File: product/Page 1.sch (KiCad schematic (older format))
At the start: 36 parts, among them J1 10118192-0001LF, J2 ARJM11A3, U1 AZ1117-3.3, U2 LAN8720A

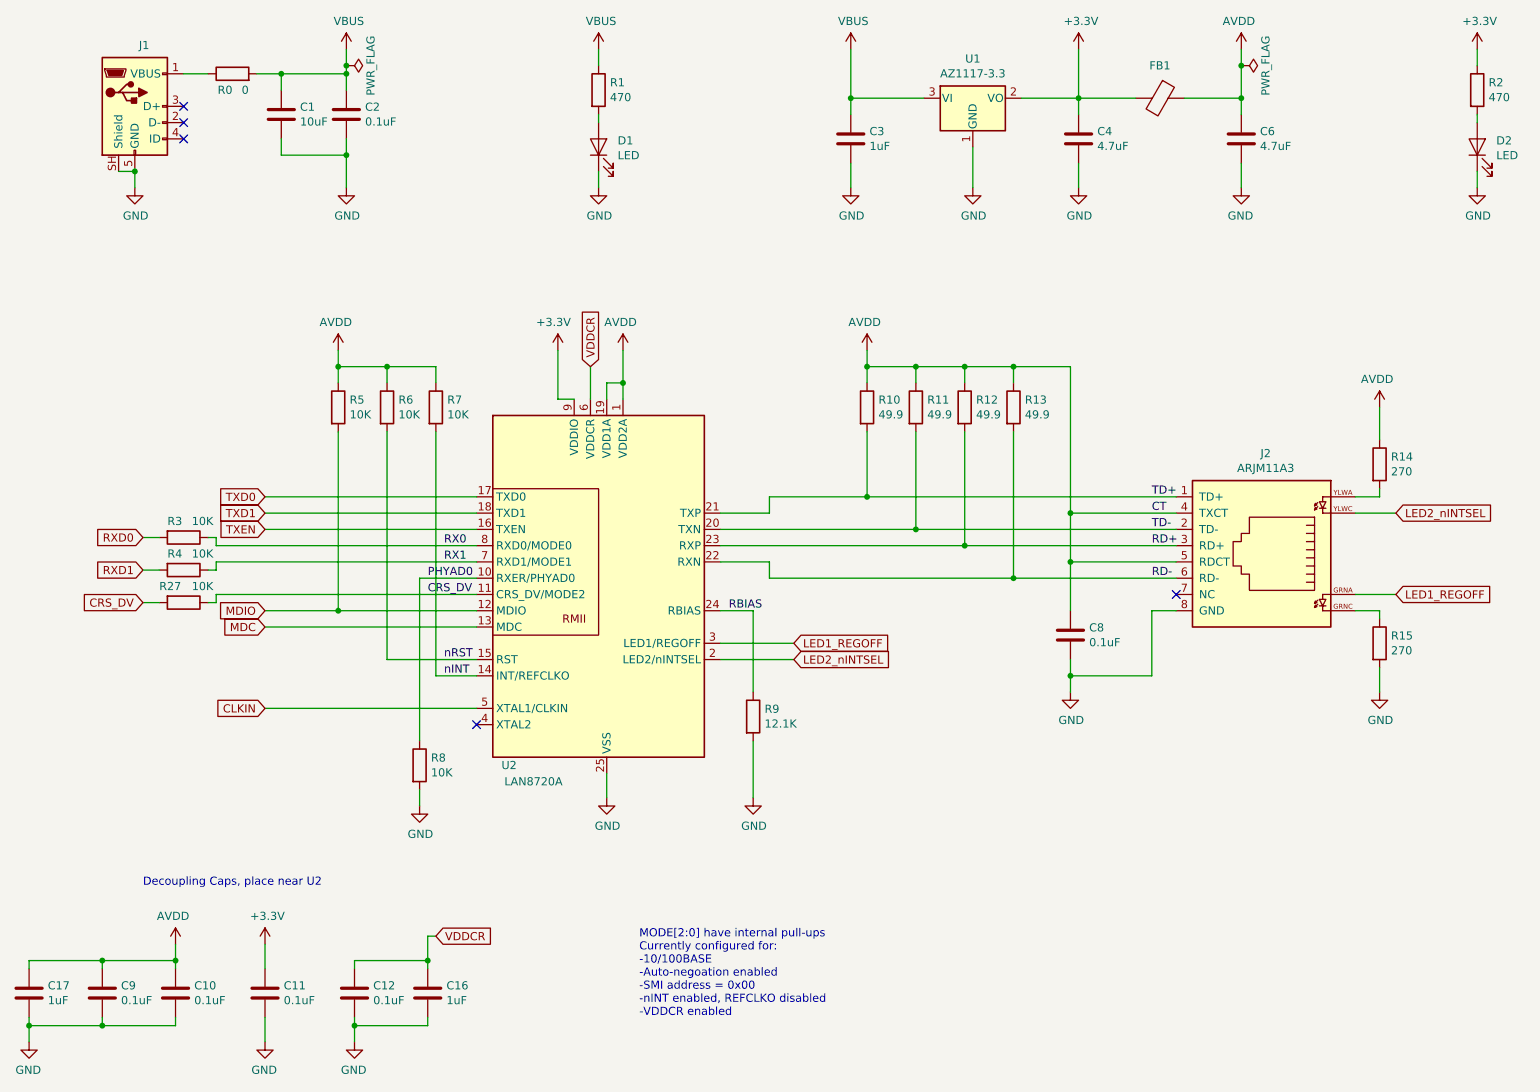
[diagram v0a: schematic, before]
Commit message: Added LCSC part numbers for product board
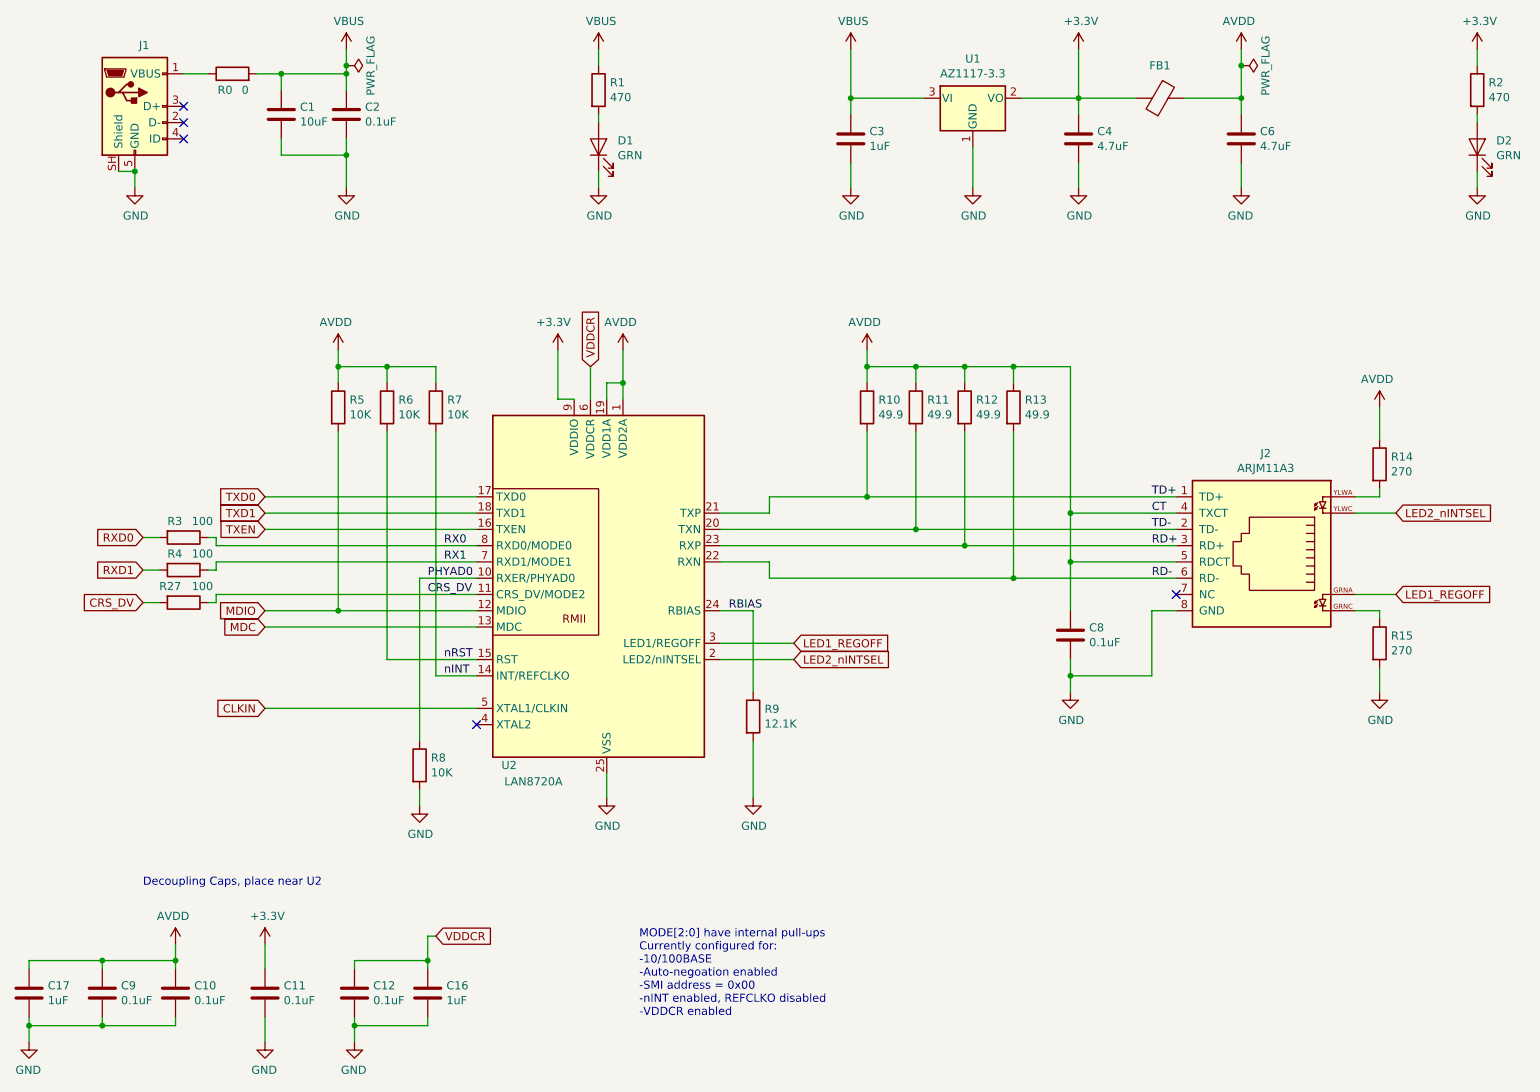
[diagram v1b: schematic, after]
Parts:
- C1: LCSC Part Number (none) -> C77044
- C10, C11, C12, C2, C8, C9: LCSC Part Number (none) -> C24452
- C16, C17, C3: LCSC Part Number (none) -> C1525
- C4, C6: LCSC Part Number (none) -> C99226
- D1, D2: value LED -> GRN; LCSC Part Number (none) -> C125094
- FB1: LCSC Part Number (none) -> C82850
- J1: LCSC Part Number (none) -> C132564
- R0: LCSC Part Number (none) -> C95177
- R1, R2: LCSC Part Number (none) -> C114433
- R10, R11, R12, R13: LCSC Part Number (none) -> C114625
- R14, R15: LCSC Part Number (none) -> C137641
- R27, R3, R4: value 10K -> 100; LCSC Part Number (none) -> C105588
- R5, R6, R7, R8: LCSC Part Number (none) -> C99198
- R9: LCSC Part Number (none) -> C123417
- U1: LCSC Part Number (none) -> C92517
- U2: LCSC Part Number (none) -> C45223
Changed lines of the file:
@@
 EESchema Schematic File Version 4
-LIBS:EsperDNS-cache
 EELAYER 30 0
 EELAYER END
@@
 F 2 "Capacitor_SMD:C_0603_1608Metric" H 2688 1500 50  0001 C CNN
 F 3 "~" H 2650 1650 50  0001 C CNN
+F 4 "C77044" H 2650 1650 50  0001 C CNN "LCSC Part Number"
 	1    2650 1650
 	1    0    0    -1
@@
 F 2 "Capacitor_SMD:C_0603_1608Metric" H 3088 1500 50  0001 C CNN
 F 3 "~" H 3050 1650 50  0001 C CNN
+F 4 "C24452" H 3050 1650 50  0001 C CNN "LCSC Part Number"
 	1    3050 1650
 	1    0    0    -1
@@
 F 2 "Resistor_SMD:R_0603_1608Metric" V 4530 1500 50  0001 C CNN
 F 3 "~" H 4600 1500 50  0001 C CNN
+F 4 "C114433" H 4600 1500 50  0001 C CNN "LCSC Part Number"
 	1    4600 1500
 	1    0    0    -1
@@
 AR Path="/5DED2F9B/5DF04BE6" Ref="D1"  Part="1"
 F 0 "D1" V 4639 1733 50  0000 R CNN
-F 1 "LED" V 4548 1733 50  0000 R CNN
+F 1 "GRN" V 4548 1733 50  0000 R CNN
 F 2 "Diode_SMD:D_0603_1608Metric" H 4600 1850 50  0001 C CNN
 F 3 "~" H 4600 1850 50  0001 C CNN
+F 4 "C125094" H 4600 1850 50  0001 C CNN "LCSC Part Number"
 	1    4600 1850
 	0    -1   -1   0
@@
 F 2 "Package_TO_SOT_SMD:SOT-223" H 6900 1800 50  0001 C CIN
 F 3 "https://www.diodes.com/assets/Datasheets/AZ1117.pdf" H 6900 1550 50  0001 C CNN
+F 4 "C92517" H 6900 1550 50  0001 C CNN "LCSC Part Number"
 	1    6900 1550
 	1    0    0    -1
@@
 F 2 "Capacitor_SMD:C_0603_1608Metric" H 6188 1650 50  0001 C CNN
 F 3 "~" H 6150 1800 50  0001 C CNN
+F 4 "C1525" H 6150 1800 50  0001 C CNN "LCSC Part Number"
 	1    6150 1800
 	1    0    0    -1
@@
 F 2 "Inductor_SMD:L_0603_1608Metric" V 7980 1550 50  0001 C CNN
 F 3 "~" H 8050 1550 50  0001 C CNN
+F 4 "C82850" H 8050 1550 50  0001 C CNN "LCSC Part Number"
 	1    8050 1550
 	0    1    1    0
@@
 F 2 "Capacitor_SMD:C_0603_1608Metric" H 7588 1650 50  0001 C CNN
 F 3 "~" H 7550 1800 50  0001 C CNN
+F 4 "C99226" H 7550 1800 50  0001 C CNN "LCSC Part Number"
 	1    7550 1800
 	1    0    0    -1
@@
 F 2 "Resistor_SMD:R_0603_1608Metric" V 9930 1500 50  0001 C CNN
 F 3 "~" H 10000 1500 50  0001 C CNN
+F 4 "C114433" H 10000 1500 50  0001 C CNN "LCSC Part Number"
 	1    10000 1500
 	1    0    0    -1
@@
 AR Path="/5DED2F9B/5DF04C4F" Ref="D2"  Part="1"
 F 0 "D2" V 10039 1733 50  0000 R CNN
-F 1 "LED" V 9948 1733 50  0000 R CNN
+F 1 "GRN" V 9948 1733 50  0000 R CNN
 F 2 "Diode_SMD:D_0603_1608Metric" H 10000 1850 50  0001 C CNN
 F 3 "~" H 10000 1850 50  0001 C CNN
+F 4 "C125094" H 10000 1850 50  0001 C CNN "LCSC Part Number"
 	1    10000 1850
 	0    -1   -1   0
@@
 F 2 "Package_DFN_QFN:QFN-24-1EP_4x4mm_P0.5mm_EP2.6x2.6mm" H 4700 3550 50  0001 L CNN
 F 3 "http://ww1.microchip.com/downloads/en/DeviceDoc/8720a.pdf" H 4450 3650 50  0001 C CNN
+F 4 "C45223" H 4650 4600 50  0001 C CNN "LCSC Part Number"
 	1    4650 4600
 	1    0    0    -1
@@
 F 2 "Resistor_SMD:R_0603_1608Metric" V 6480 3450 50  0001 C CNN
 F 3 "~" H 6550 3450 50  0001 C CNN
+F 4 "C114625" H 6550 3450 50  0001 C CNN "LCSC Part Number"
 	1    6550 3450
 	1    0    0    -1
@@
 F 2 "Resistor_SMD:R_0603_1608Metric" V 6780 3450 50  0001 C CNN
 F 3 "~" H 6850 3450 50  0001 C CNN
+F 4 "C114625" H 6850 3450 50  0001 C CNN "LCSC Part Number"
 	1    6850 3450
 	1    0    0    -1
@@
 F 2 "Resistor_SMD:R_0603_1608Metric" V 6180 3450 50  0001 C CNN
 F 3 "~" H 6250 3450 50  0001 C CNN
+F 4 "C114625" H 6250 3450 50  0001 C CNN "LCSC Part Number"
 	1    6250 3450
 	1    0    0    -1
@@
 F 2 "Resistor_SMD:R_0603_1608Metric" V 9330 3800 50  0001 C CNN
 F 3 "~" H 9400 3800 50  0001 C CNN
+F 4 "C137641" H 9400 3800 50  0001 C CNN "LCSC Part Number"
 	1    9400 3800
 	1    0    0    -1
@@
 F 2 "Resistor_SMD:R_0603_1608Metric" V 9330 4900 50  0001 C CNN
 F 3 "~" H 9400 4900 50  0001 C CNN
+F 4 "C137641" H 9400 4900 50  0001 C CNN "LCSC Part Number"
 	1    9400 4900
 	1    0    0    -1
@@
 F 2 "Capacitor_SMD:C_0603_1608Metric" H 7538 4700 50  0001 C CNN
 F 3 "~" H 7500 4850 50  0001 C CNN
+F 4 "C24452" H 7500 4850 50  0001 C CNN "LCSC Part Number"
 	1    7500 4850
 	-1   0    0    -1
@@
 F 2 "Resistor_SMD:R_0603_1608Metric" V 5480 5350 50  0001 C CNN
 F 3 "~" H 5550 5350 50  0001 C CNN
+F 4 "C123417" H 5550 5350 50  0001 C CNN "LCSC Part Number"
 	1    5550 5350
 	1    0    0    -1
@@
 F 2 "Resistor_SMD:R_0603_1608Metric" V 3430 5650 50  0001 C CNN
 F 3 "~" H 3500 5650 50  0001 C CNN
+F 4 "C99198" H 3500 5650 50  0001 C CNN "LCSC Part Number"
 	1    3500 5650
 	1    0    0    -1
@@
 F 2 "Resistor_SMD:R_0603_1608Metric" V 7080 3450 50  0001 C CNN
 F 3 "~" H 7150 3450 50  0001 C CNN
+F 4 "C114625" H 7150 3450 50  0001 C CNN "LCSC Part Number"
 	1    7150 3450
 	1    0    0    -1
@@
 F 2 "Capacitor_SMD:C_0603_1608Metric" H 8588 1650 50  0001 C CNN
 F 3 "~" H 8550 1800 50  0001 C CNN
+F 4 "C99226" H 8550 1800 50  0001 C CNN "LCSC Part Number"
 	1    8550 1800
 	-1   0    0    -1
@@
 F 2 "Resistor_SMD:R_0603_1608Metric" V 3530 3450 50  0001 C CNN
 F 3 "~" H 3600 3450 50  0001 C CNN
+F 4 "C99198" H 3600 3450 50  0001 C CNN "LCSC Part Number"
 	1    3600 3450
 	1    0    0    -1
@@
 F 2 "Resistor_SMD:R_0603_1608Metric" V 3230 3450 50  0001 C CNN
 F 3 "~" H 3300 3450 50  0001 C CNN
+F 4 "C99198" H 3300 3450 50  0001 C CNN "LCSC Part Number"
 	1    3300 3450
 	1    0    0    -1
@@
 F 2 "Resistor_SMD:R_0603_1608Metric" V 2930 3450 50  0001 C CNN
 F 3 "~" H 3000 3450 50  0001 C CNN
+F 4 "C99198" H 3000 3450 50  0001 C CNN "LCSC Part Number"
 	1    3000 3450
 	1    0    0    -1
@@
 F 2 "Resistor_SMD:R_0603_1608Metric" V 2280 1400 50  0001 C CNN
 F 3 "~" H 2350 1400 50  0001 C CNN
+F 4 "C95177" H 2350 1400 50  0001 C CNN "LCSC Part Number"
 	1    2350 1400
 	0    -1   -1   0
@@
 F 2 "Capacitor_SMD:C_0603_1608Metric" H 2038 6900 50  0001 C CNN
 F 3 "~" H 2000 7050 50  0001 C CNN
+F 4 "C24452" H 2000 7050 50  0001 C CNN "LCSC Part Number"
 	1    2000 7050
 	-1   0    0    -1
@@
 F 2 "Capacitor_SMD:C_0603_1608Metric" H 1588 6900 50  0001 C CNN
 F 3 "~" H 1550 7050 50  0001 C CNN
+F 4 "C24452" H 1550 7050 50  0001 C CNN "LCSC Part Number"
 	1    1550 7050
 	-1   0    0    -1
@@
 F 2 "Capacitor_SMD:C_0603_1608Metric" H 2588 6900 50  0001 C CNN
 F 3 "~" H 2550 7050 50  0001 C CNN
+F 4 "C24452" H 2550 7050 50  0001 C CNN "LCSC Part Number"
 	1    2550 7050
 	-1   0    0    -1
@@
 F 2 "Capacitor_SMD:C_0603_1608Metric" H 3138 6900 50  0001 C CNN
 F 3 "~" H 3100 7050 50  0001 C CNN
+F 4 "C24452" H 3100 7050 50  0001 C CNN "LCSC Part Number"
 	1    3100 7050
 	-1   0    0    -1
@@
 AR Path="/5DED2F9B/5DFE68F0" Ref="R3"  Part="1"
 F 0 "R3" V 1950 4150 50  0000 L CNN
-F 1 "10K" V 1950 4300 50  0000 L CNN
+F 1 "100" V 1950 4300 50  0000 L CNN
 F 2 "Resistor_SMD:R_0603_1608Metric" V 1980 4250 50  0001 C CNN
 F 3 "~" H 2050 4250 50  0001 C CNN
+F 4 "C105588" H 2050 4250 50  0001 C CNN "LCSC Part Number"
 	1    2050 4250
 	0    1    1    0
@@
 AR Path="/5DED2F9B/5DFE6B8F" Ref="R4"  Part="1"
 F 0 "R4" V 1950 4350 50  0000 L CNN
-F 1 "10K" V 1950 4500 50  0000 L CNN
+F 1 "100" V 1950 4500 50  0000 L CNN
 F 2 "Resistor_SMD:R_0603_1608Metric" V 1980 4450 50  0001 C CNN
 F 3 "~" H 2050 4450 50  0001 C CNN
+F 4 "C105588" H 2050 4450 50  0001 C CNN "LCSC Part Number"
 	1    2050 4450
 	0    1    1    0
@@
 F 2 "digikey-footprints:USB_Micro_B_Female_10118192" H 1900 1550 50  0001 C CNN
 F 3 "~" H 1900 1550 50  0001 C CNN
+F 4 "C132564" H 1750 1600 50  0001 C CNN "LCSC Part Number"
 	1    1750 1600
 	1    0    0    -1
@@
 F 2 "Capacitor_SMD:C_0603_1608Metric" H 3588 6900 50  0001 C CNN
 F 3 "~" H 3550 7050 50  0001 C CNN
+F 4 "C1525" H 3550 7050 50  0001 C CNN "LCSC Part Number"
 	1    3550 7050
 	-1   0    0    -1
@@
 F 2 "Capacitor_SMD:C_0603_1608Metric" H 1138 6900 50  0001 C CNN
 F 3 "~" H 1100 7050 50  0001 C CNN
+F 4 "C1525" H 1100 7050 50  0001 C CNN "LCSC Part Number"
 	1    1100 7050
 	-1   0    0    -1
@@
 AR Path="/5DED2F9B/5DFF908E" Ref="R27"  Part="1"
 F 0 "R27" V 1950 4500 50  0000 L CNN
-F 1 "10K" V 1950 4700 50  0000 L CNN
+F 1 "100" V 1950 4700 50  0000 L CNN
 F 2 "Resistor_SMD:R_0603_1608Metric" V 1980 4650 50  0001 C CNN
 F 3 "~" H 2050 4650 50  0001 C CNN
+F 4 "C105588" H 2050 4650 50  0001 C CNN "LCSC Part Number"
 	1    2050 4650
 	0    1    1    0

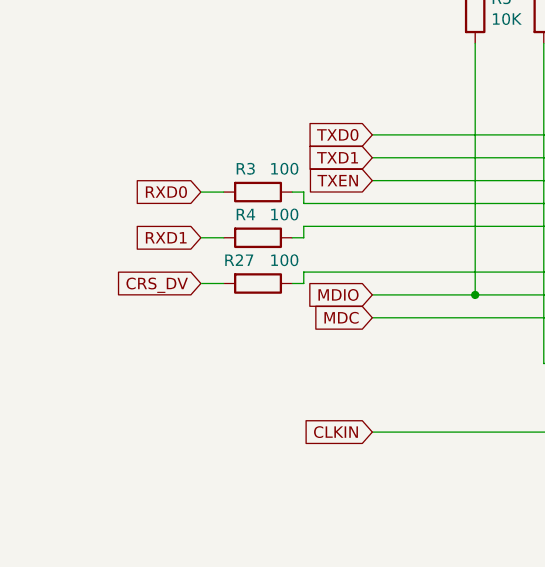
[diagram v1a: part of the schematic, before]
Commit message: Swapped TX & RX on Product Board
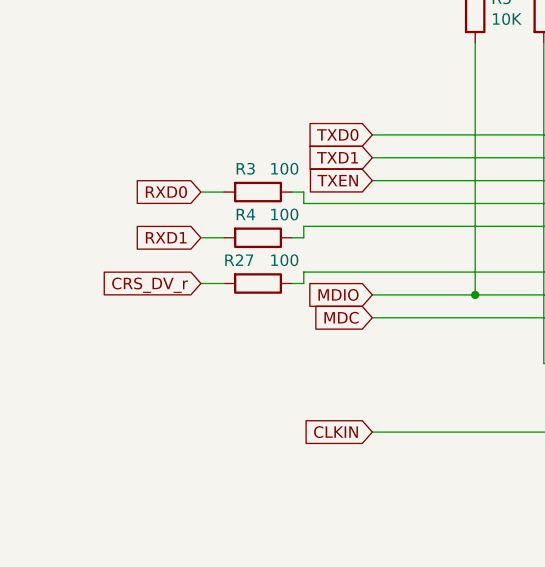
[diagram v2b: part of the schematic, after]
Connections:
- net CRS_DV: no longer R27.2
- new net CRS_DV_r: R27.2
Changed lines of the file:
@@
 MDIO
 Text GLabel 1800 4650 0    50   Input ~ 0
-CRS_DV
+CRS_DV_r
 Text GLabel 1800 4450 0    50   Input ~ 0
 RXD1
@@
 $EndComp
 Wire Wire Line
-	3500 4500 3500 5500
-Wire Wire Line
 	3500 5900 3500 5800
 $Comp
@@
 Wire Wire Line
 	2250 4650 2250 4600
-Wire Wire Line
-	2250 4600 3850 4600
 $Comp
 L Device:R R?
@@
 Text Label 3650 4400 0    50   ~ 0
 RX1
-Text Label 3550 4600 0    50   ~ 0
-CRS_DV
 $Comp
 L power:+3.3V #PWR?
@@
 	1    0    0    -1
 $EndComp
+Wire Wire Line
+	3500 4500 3500 5500
+Wire Wire Line
+	2250 4600 3850 4600
+Text Label 3550 4600 0    50   ~ 0
+CRS_DV
 $EndSCHEMATC

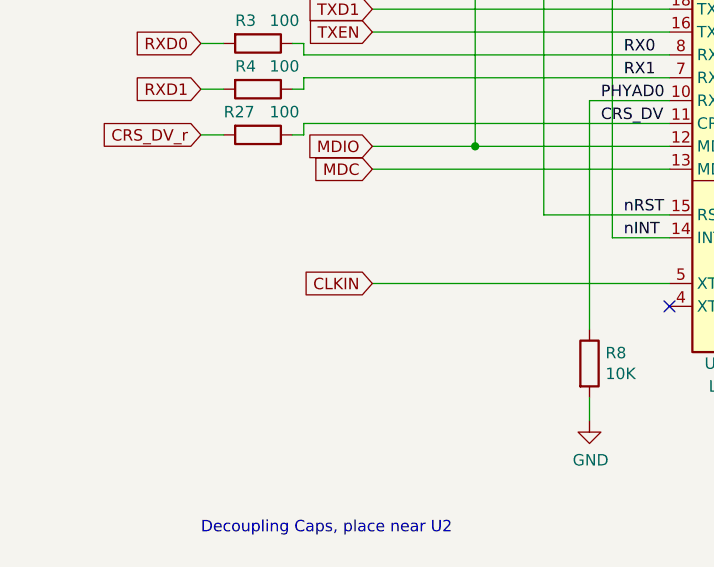
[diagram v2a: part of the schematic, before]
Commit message: Removed oscillator, replaced with IO17
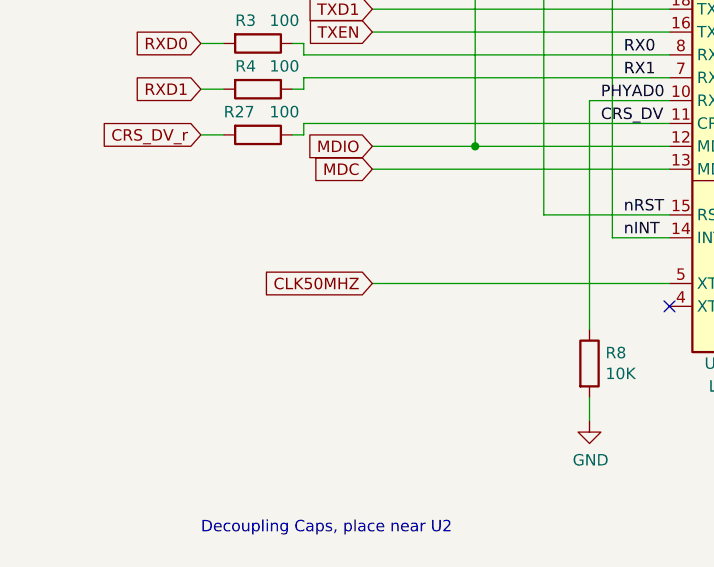
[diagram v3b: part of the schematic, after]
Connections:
- net CLKIN renamed CLK50MHZ
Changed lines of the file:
@@
 TXD0
 Text GLabel 2550 5300 0    50   Input ~ 0
-CLKIN
+CLK50MHZ
 $Comp
 L Device:R R?
